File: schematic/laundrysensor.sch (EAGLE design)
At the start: 12 parts, among them J1 Adafruit I2S amplifier MAX983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

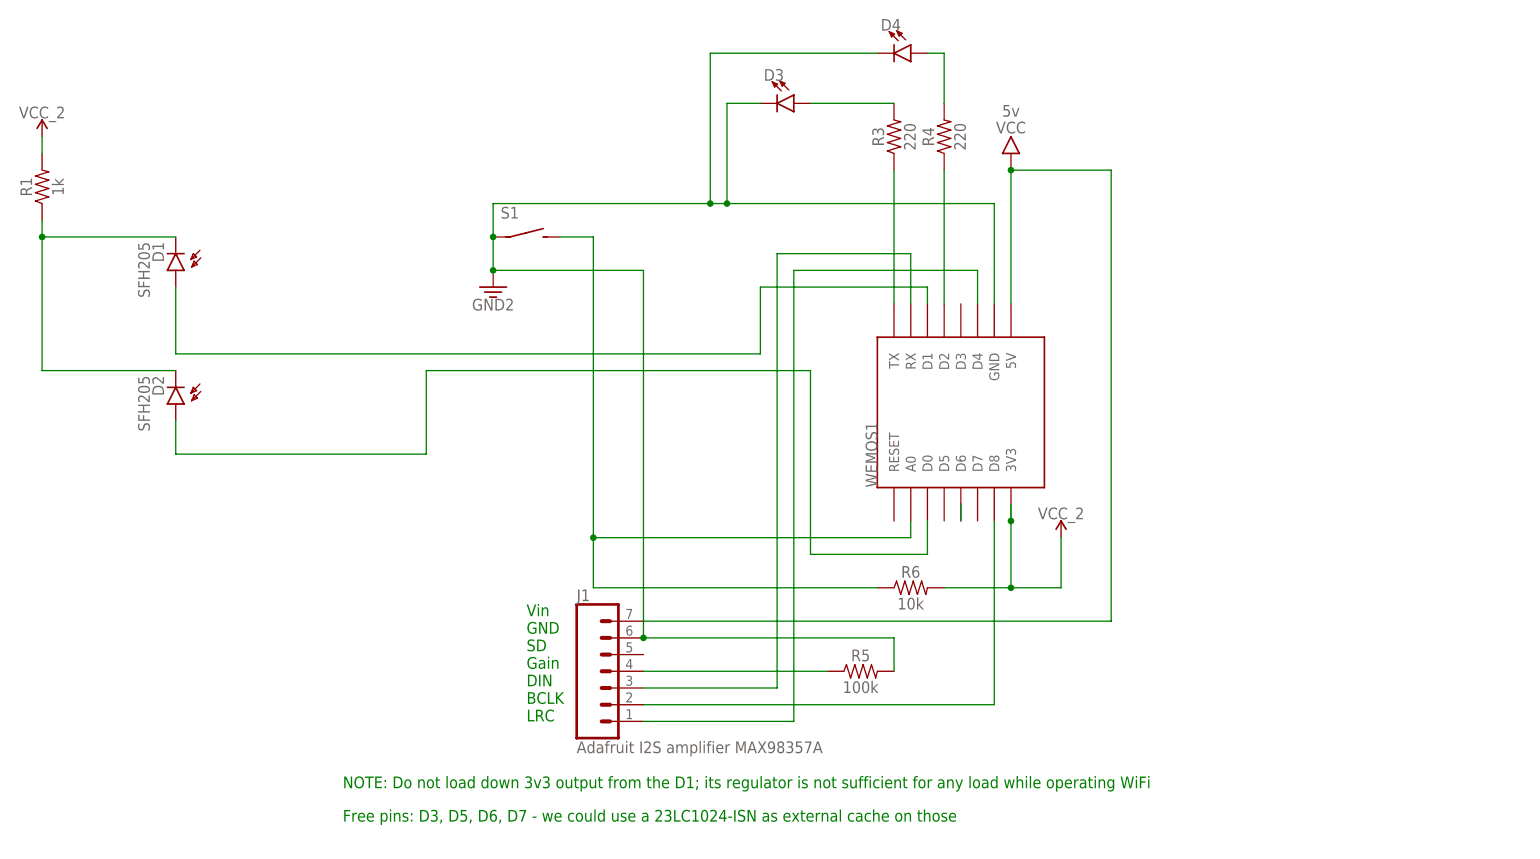
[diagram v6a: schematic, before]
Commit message: esp32-s3 version work in progress
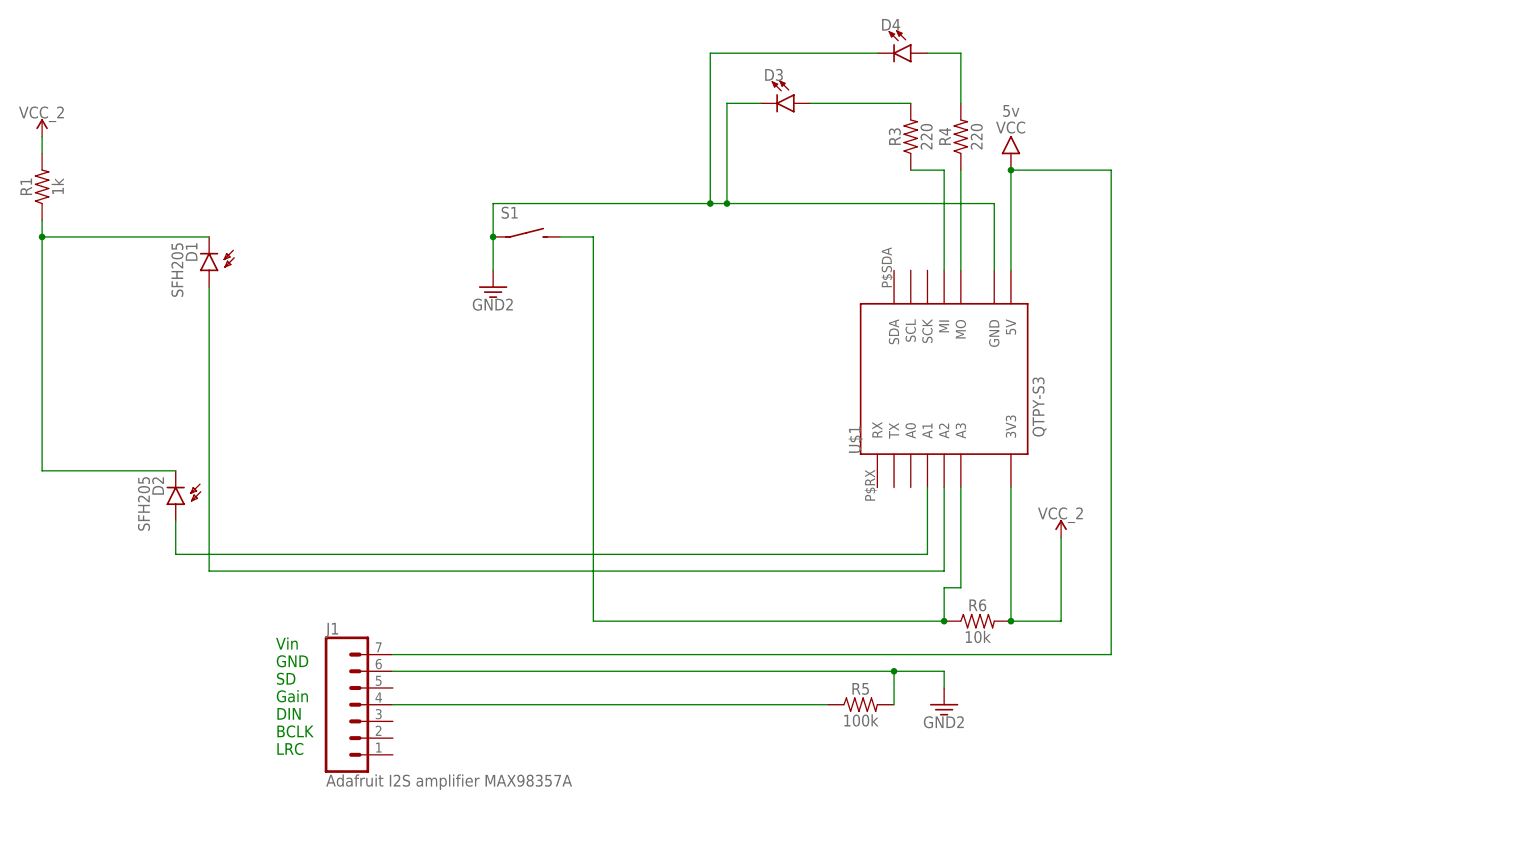
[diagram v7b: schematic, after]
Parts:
- removed WEMOS1: (no value), esp8266modules:WEMOS-D1-MINI
- added U$1: QTPY-S3, jorjlib:QTPY-S3
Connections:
- removed net N$10: J1.1, WEMOS1.D4
- removed net N$11: WEMOS1.D6
- removed net N$13: R3.1, WEMOS1.TX
- removed net N$8: J1.3, WEMOS1.RX
- removed net N$9: J1.2, WEMOS1.D8
- new net N$1: R4.1, U$1.MO
- net 3.3V: now also U$1.GND; no longer WEMOS1.GND
- net N$2: now also R3.1, U$1.MI; no longer R4.1, WEMOS1.D2
- net N$3: now also U$1.A1; no longer WEMOS1.D0
- net N$4: now also U$1.A3; no longer WEMOS1.A0
- net N$5: now also U$1.A2; no longer WEMOS1.D1
- net VCC: now also U$1.5V; no longer WEMOS1.5V
- net VCC_2: now also U$1.3V3; no longer WEMOS1.3V3
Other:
- note removed: "Free pins: D3, D5, D6, D7 - we could use a 23LC1024-ISN as external cache on those"
- note removed: "NOTE: Do not load down 3v3 output from the D1; its regulator is not sufficient for any load while operating WiFi"
- moved on the sheet: D1, D2, J1, R3, R4, R5, R6

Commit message: update
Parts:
- added R2, R7: 1k, SparkFun-Resistors:1KOHM-HORIZ-1/4W-5%
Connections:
- new net N$6: D2.A, R2.2
- new net N$8: R7.1, U$1.A2
- net N$3: now also R2.1; no longer D2.A
- net N$5: now also R7.2; no longer U$1.A2
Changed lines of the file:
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@@
 <part name="U$1" library="jorjlib" deviceset="QTPY-S3" device=""/>
 <part name="GND1" library="SparkFun-PowerSymbols" deviceset="GND2" device=""/>
+<part name="R2" library="SparkFun-Resistors" deviceset="1KOHM" device="-HORIZ-1/4W-5%" value="1k"/>
+<part name="R7" library="SparkFun-Resistors" deviceset="1KOHM" device="-HORIZ-1/4W-5%" value="1k"/>
 </parts>
 <sheets>
@@
 <attribute name="VALUE" x="162.56" y="41.402" size="1.778" layer="96" align="top-center"/>
 </instance>
+<instance part="R2" gate="G$1" x="71.12" y="66.04" smashed="yes" rot="R180">
+<attribute name="NAME" x="71.12" y="64.516" size="1.778" layer="95" font="vector" rot="R180" align="bottom-center"/>
+<attribute name="VALUE" x="71.12" y="67.564" size="1.778" layer="96" font="vector" rot="R180" align="top-center"/>
+</instance>
+<instance part="R7" gate="G$1" x="86.36" y="63.5" smashed="yes" rot="R180">
+<attribute name="NAME" x="86.36" y="61.976" size="1.778" layer="95" font="vector" rot="R180" align="bottom-center"/>
+<attribute name="VALUE" x="86.36" y="65.024" size="1.778" layer="96" font="vector" rot="R180" align="top-center"/>
+</instance>
 </instances>
 <busses>
@@
 <net name="N$3" class="0">
 <segment>
-<pinref part="D2" gate="1" pin="A"/>
-<wire x1="45.72" y1="66.04" x2="45.72" y2="71.12" width="0.1524" layer="91"/>
 <pinref part="U$1" gate="G$1" pin="A1"/>
 <wire x1="160.02" y1="76.2" x2="160.02" y2="66.04" width="0.1524" layer="91"/>
-<wire x1="160.02" y1="66.04" x2="45.72" y2="66.04" width="0.1524" layer="91"/>
+<pinref part="R2" gate="G$1" pin="1"/>
+<wire x1="76.2" y1="66.04" x2="160.02" y2="66.04" width="0.1524" layer="91"/>
 </segment>
 </net>
@@
 <pinref part="D1" gate="1" pin="A"/>
 <wire x1="50.8" y1="63.5" x2="50.8" y2="106.68" width="0.1524" layer="91"/>
-<pinref part="U$1" gate="G$1" pin="A2"/>
-<wire x1="162.56" y1="76.2" x2="162.56" y2="63.5" width="0.1524" layer="91"/>
-<wire x1="162.56" y1="63.5" x2="50.8" y2="63.5" width="0.1524" layer="91"/>
+<pinref part="R7" gate="G$1" pin="2"/>
+<wire x1="81.28" y1="63.5" x2="50.8" y2="63.5" width="0.1524" layer="91"/>
 </segment>
 </net>
@@
 </segment>
 </net>
+<net name="N$6" class="0">
+<segment>
+<pinref part="D2" gate="1" pin="A"/>
+<wire x1="45.72" y1="66.04" x2="45.72" y2="71.12" width="0.1524" layer="91"/>
+<pinref part="R2" gate="G$1" pin="2"/>
+<wire x1="45.72" y1="66.04" x2="66.04" y2="66.04" width="0.1524" layer="91"/>
+</segment>
+</net>
+<net name="N$8" class="0">
+<segment>
+<pinref part="U$1" gate="G$1" pin="A2"/>
+<wire x1="162.56" y1="76.2" x2="162.56" y2="63.5" width="0.1524" layer="91"/>
+<pinref part="R7" gate="G$1" pin="1"/>
+<wire x1="162.56" y1="63.5" x2="91.44" y2="63.5" width="0.1524" layer="91"/>
+</segment>
+</net>
